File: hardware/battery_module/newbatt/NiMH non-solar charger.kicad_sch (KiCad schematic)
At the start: 23 parts, among them J14 Conn_01x01_Socket, J15 Conn_01x01_Socket, J16 Conn_01x01_Socket, J17 Conn_01x01_Socket, J18 Conn_01x01_Socket, J19 Conn_01x01_Socket, J20 Conn_01x01_Socket, J21 Conn_01x01_Socket, J4 Screw_Terminal_01x02, U1 BQ25172DSGR

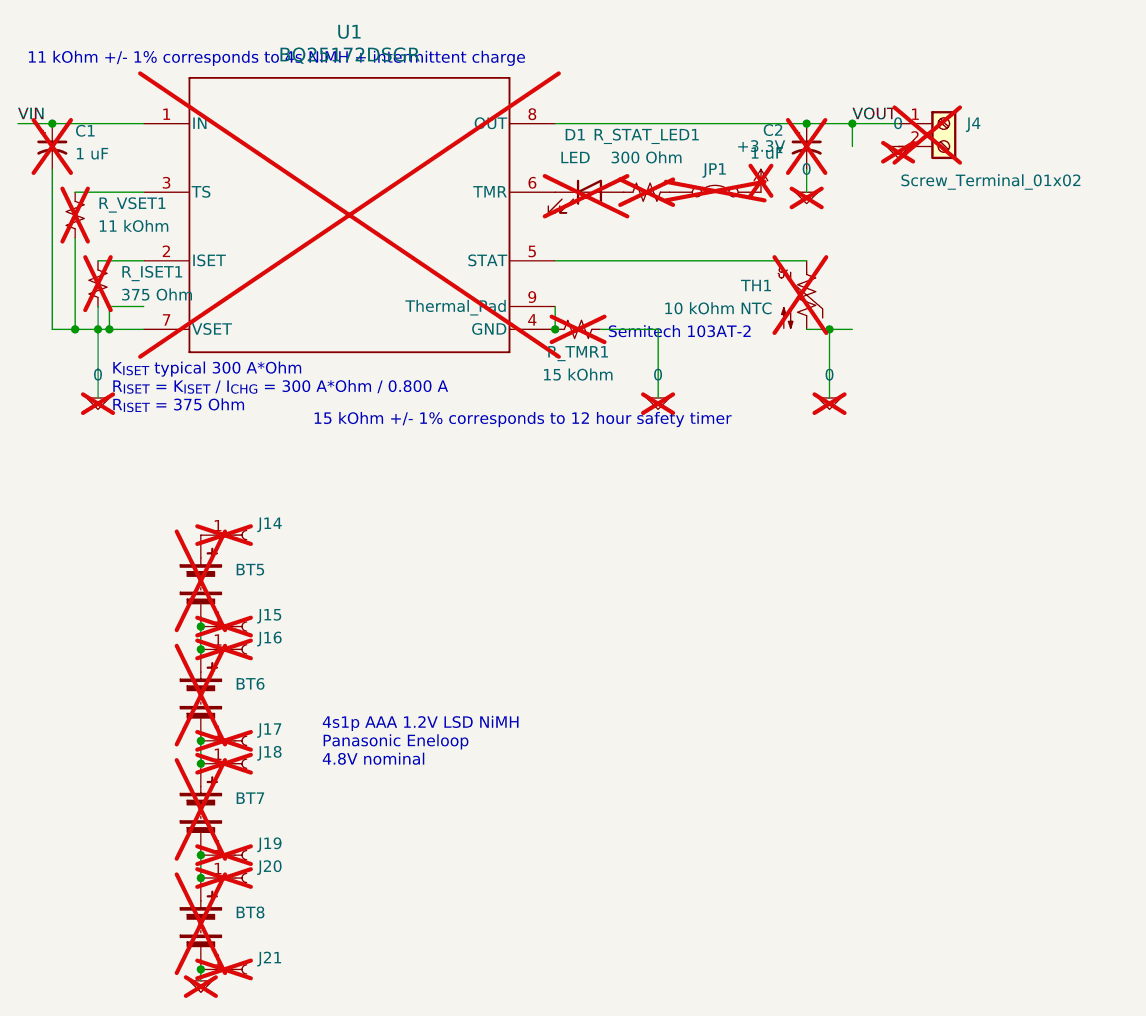
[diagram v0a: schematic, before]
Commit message: battery switch, fuse, and rerouted traces
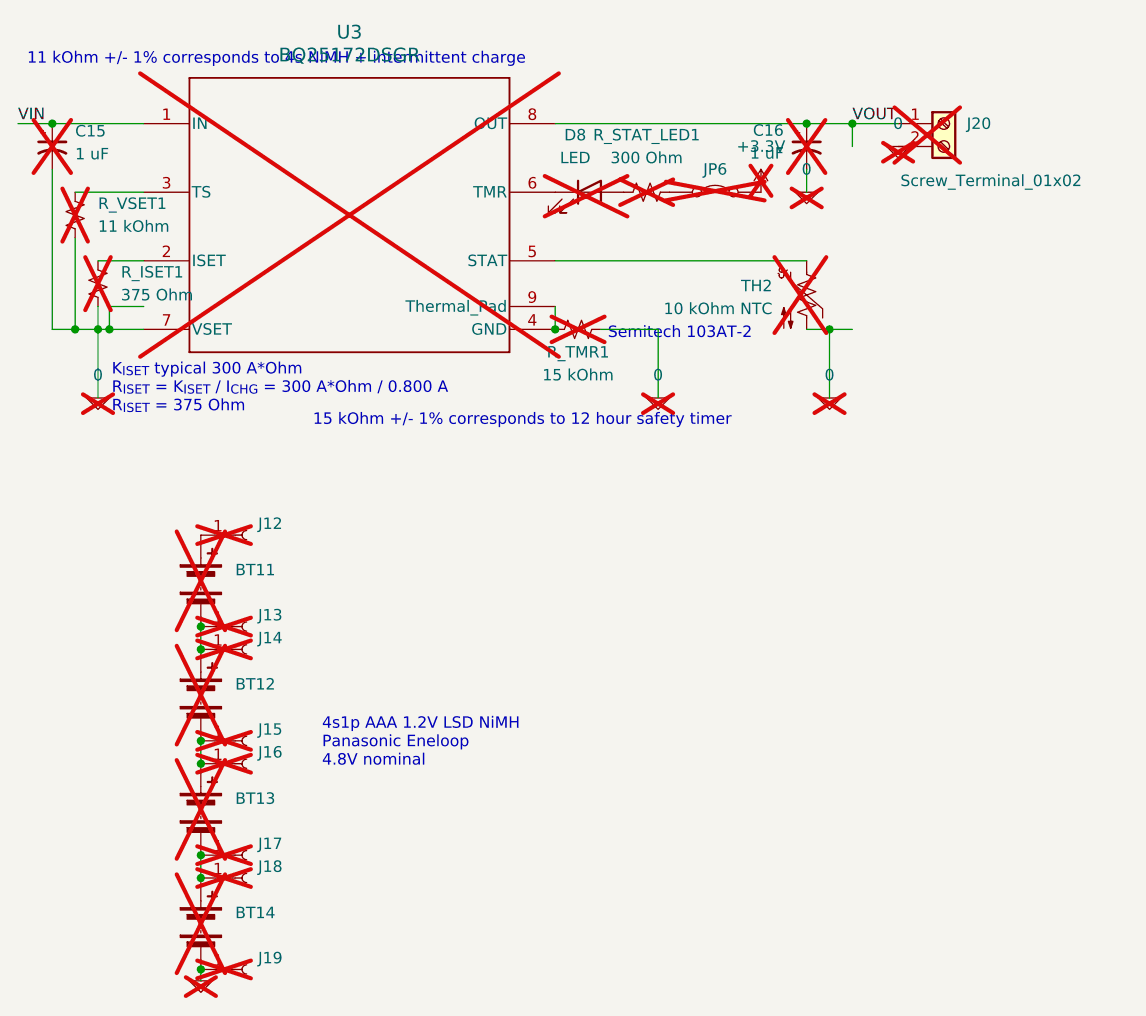
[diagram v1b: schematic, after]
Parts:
- renumbered BT5 to BT11, BT6 to BT12, BT7 to BT13, BT8 to BT14, C1 to C15, C2 to C16, D1 to D8, J14 to J12, J15 to J13, J16 to J14, J17 to J15, J18 to J16, J19 to J17, J20 to J18, J21 to J19, J4 to J20, JP1 to JP6, TH1 to TH2, U1 to U3
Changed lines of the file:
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@@
 		(dnp yes)
 		(fields_autoplaced yes)
-		(property "Reference" "#GND011"
+		(property "Reference" "#GND036"
 			(at 168.91 85.09 0)
 			(effects
@@
 			(project "newbatt"
 				(path "/492e8d1d-dcc5-45c6-a3d2-2dfd8a06477e/93fd5e6a-f298-4a43-8a46-dea204637830"
-					(reference "#GND011")
+					(reference "#GND036")
 					(unit 1)
 				)
@@
 		(on_board no)
 		(dnp yes)
-		(property "Reference" "JP1"
+		(property "Reference" "JP6"
 			(at 148.59 82.55 0)
 			(effects
@@
 			(project "newbatt"
 				(path "/492e8d1d-dcc5-45c6-a3d2-2dfd8a06477e/93fd5e6a-f298-4a43-8a46-dea204637830"
-					(reference "JP1")
+					(reference "JP6")
 					(unit 1)
 				)
@@
 		(dnp yes)
 		(fields_autoplaced yes)
-		(property "Reference" "#GND04"
+		(property "Reference" "#GND035"
 			(at 161.29 113.03 0)
 			(effects
@@
 			(project "newbatt"
 				(path "/492e8d1d-dcc5-45c6-a3d2-2dfd8a06477e/93fd5e6a-f298-4a43-8a46-dea204637830"
-					(reference "#GND04")
+					(reference "#GND035")
 					(unit 1)
 				)
@@
 		(dnp yes)
 		(fields_autoplaced yes)
-		(property "Reference" "J20"
+		(property "Reference" "J18"
 			(at 97.79 160.0199 0)
 			(effects
@@
 			(project "newbatt"
 				(path "/492e8d1d-dcc5-45c6-a3d2-2dfd8a06477e/93fd5e6a-f298-4a43-8a46-dea204637830"
-					(reference "J20")
+					(reference "J18")
 					(unit 1)
 				)
@@
 		(dnp yes)
 		(fields_autoplaced yes)
-		(property "Reference" "J15"
+		(property "Reference" "J13"
 			(at 97.79 132.0799 0)
 			(effects
@@
 			(project "newbatt"
 				(path "/492e8d1d-dcc5-45c6-a3d2-2dfd8a06477e/93fd5e6a-f298-4a43-8a46-dea204637830"
-					(reference "J15")
+					(reference "J13")
 					(unit 1)
 				)
@@
 		(dnp yes)
 		(fields_autoplaced yes)
-		(property "Reference" "#GND01"
+		(property "Reference" "#GND031"
 			(at 80.01 113.03 0)
 			(effects
@@
 			(project "newbatt"
 				(path "/492e8d1d-dcc5-45c6-a3d2-2dfd8a06477e/93fd5e6a-f298-4a43-8a46-dea204637830"
-					(reference "#GND01")
+					(reference "#GND031")
 					(unit 1)
 				)
@@
 		(on_board no)
 		(dnp yes)
-		(property "Reference" "C2"
+		(property "Reference" "C16"
 			(at 156.21 78.232 0)
 			(effects
@@
 			(project "newbatt"
 				(path "/492e8d1d-dcc5-45c6-a3d2-2dfd8a06477e/93fd5e6a-f298-4a43-8a46-dea204637830"
-					(reference "C2")
+					(reference "C16")
 					(unit 1)
 				)
@@
 		(dnp yes)
 		(fields_autoplaced yes)
-		(property "Reference" "#GND03"
+		(property "Reference" "#GND034"
 			(at 158.75 90.17 0)
 			(effects
@@
 			(project "newbatt"
 				(path "/492e8d1d-dcc5-45c6-a3d2-2dfd8a06477e/93fd5e6a-f298-4a43-8a46-dea204637830"
-					(reference "#GND03")
+					(reference "#GND034")
 					(unit 1)
 				)
@@
 		(dnp yes)
 		(fields_autoplaced yes)
-		(property "Reference" "D1"
+		(property "Reference" "D8"
 			(at 133.0325 78.74 0)
 			(effects
@@
 			(project "newbatt"
 				(path "/492e8d1d-dcc5-45c6-a3d2-2dfd8a06477e/93fd5e6a-f298-4a43-8a46-dea204637830"
-					(reference "D1")
+					(reference "D8")
 					(unit 1)
 				)
@@
 		(dnp yes)
 		(fields_autoplaced yes)
-		(property "Reference" "U1"
+		(property "Reference" "U3"
 			(at 107.95 67.31 0)
 			(effects
@@
 			(project "newbatt"
 				(path "/492e8d1d-dcc5-45c6-a3d2-2dfd8a06477e/93fd5e6a-f298-4a43-8a46-dea204637830"
-					(reference "U1")
+					(reference "U3")
 					(unit 1)
 				)
@@
 		(dnp yes)
 		(fields_autoplaced yes)
-		(property "Reference" "J16"
+		(property "Reference" "J14"
 			(at 97.79 134.6199 0)
 			(effects
@@
 			(project "newbatt"
 				(path "/492e8d1d-dcc5-45c6-a3d2-2dfd8a06477e/93fd5e6a-f298-4a43-8a46-dea204637830"
-					(reference "J16")
+					(reference "J14")
 					(unit 1)
 				)
@@
 		(dnp yes)
 		(fields_autoplaced yes)
-		(property "Reference" "#GND034"
+		(property "Reference" "#GND032"
 			(at 91.44 177.8 0)
 			(effects
@@
 			(project "newbatt"
 				(path "/492e8d1d-dcc5-45c6-a3d2-2dfd8a06477e/93fd5e6a-f298-4a43-8a46-dea204637830"
-					(reference "#GND034")
+					(reference "#GND032")
 					(unit 1)
 				)
@@
 		(dnp yes)
 		(fields_autoplaced yes)
-		(property "Reference" "J17"
+		(property "Reference" "J15"
 			(at 97.79 144.7799 0)
 			(effects
@@
 			(project "newbatt"
 				(path "/492e8d1d-dcc5-45c6-a3d2-2dfd8a06477e/93fd5e6a-f298-4a43-8a46-dea204637830"
-					(reference "J17")
+					(reference "J15")
 					(unit 1)
 				)
@@
 		(dnp yes)
 		(fields_autoplaced yes)
-		(property "Reference" "BT7"
+		(property "Reference" "BT13"
 			(at 95.25 152.4634 0)
 			(effects
@@
 			(project "newbatt"
 				(path "/492e8d1d-dcc5-45c6-a3d2-2dfd8a06477e/93fd5e6a-f298-4a43-8a46-dea204637830"
-					(reference "BT7")
+					(reference "BT13")
 					(unit 1)
 				)
@@
 		(dnp yes)
 		(fields_autoplaced yes)
-		(property "Reference" "J18"
+		(property "Reference" "J16"
 			(at 97.79 147.3199 0)
 			(effects
@@
 			(project "newbatt"
 				(path "/492e8d1d-dcc5-45c6-a3d2-2dfd8a06477e/93fd5e6a-f298-4a43-8a46-dea204637830"
-					(reference "J18")
+					(reference "J16")
 					(unit 1)
 				)
@@
 		(dnp yes)
 		(fields_autoplaced yes)
-		(property "Reference" "J19"
+		(property "Reference" "J17"
 			(at 97.79 157.4799 0)
 			(effects
@@
 			(project "newbatt"
 				(path "/492e8d1d-dcc5-45c6-a3d2-2dfd8a06477e/93fd5e6a-f298-4a43-8a46-dea204637830"
-					(reference "J19")
+					(reference "J17")
 					(unit 1)
 				)
@@
 		(dnp yes)
 		(fields_autoplaced yes)
-		(property "Reference" "J21"
+		(property "Reference" "J19"
 			(at 97.79 170.1799 0)
 			(effects
@@
 			(project "newbatt"
 				(path "/492e8d1d-dcc5-45c6-a3d2-2dfd8a06477e/93fd5e6a-f298-4a43-8a46-dea204637830"
-					(reference "J21")
+					(reference "J19")
 					(unit 1)
 				)
@@
 		(dnp yes)
 		(fields_autoplaced yes)
-		(property "Reference" "J14"
+		(property "Reference" "J12"
 			(at 97.79 121.9199 0)
 			(effects
@@
 			(project "newbatt"
 				(path "/492e8d1d-dcc5-45c6-a3d2-2dfd8a06477e/93fd5e6a-f298-4a43-8a46-dea204637830"
-					(reference "J14")
+					(reference "J12")
 					(unit 1)
 				)
@@
 		(dnp yes)
 		(fields_autoplaced yes)
-		(property "Reference" "BT8"
+		(property "Reference" "BT14"
 			(at 95.25 165.1634 0)
 			(effects
@@
 			(project "newbatt"
 				(path "/492e8d1d-dcc5-45c6-a3d2-2dfd8a06477e/93fd5e6a-f298-4a43-8a46-dea204637830"
-					(reference "BT8")
+					(reference "BT14")
 					(unit 1)
 				)
@@
 		(on_board no)
 		(dnp yes)
-		(property "Reference" "J4"
+		(property "Reference" "J20"
 			(at 176.53 77.4699 0)
 			(effects
@@
 			(project "newbatt"
 				(path "/492e8d1d-dcc5-45c6-a3d2-2dfd8a06477e/93fd5e6a-f298-4a43-8a46-dea204637830"
-					(reference "J4")
+					(reference "J20")
 					(unit 1)
 				)
@@
 		(dnp yes)
 		(fields_autoplaced yes)
-		(property "Reference" "BT6"
+		(property "Reference" "BT12"
 			(at 95.25 139.7634 0)
 			(effects
@@
 			(project "newbatt"
 				(path "/492e8d1d-dcc5-45c6-a3d2-2dfd8a06477e/93fd5e6a-f298-4a43-8a46-dea204637830"
-					(reference "BT6")
+					(reference "BT12")
 					(unit 1)
 				)
@@
 		(dnp yes)
 		(fields_autoplaced yes)
-		(property "Reference" "C1"
+		(property "Reference" "C15"
 			(at 77.47 78.3081 0)
 			(effects
@@
 			(project "newbatt"
 				(path "/492e8d1d-dcc5-45c6-a3d2-2dfd8a06477e/93fd5e6a-f298-4a43-8a46-dea204637830"
-					(reference "C1")
+					(reference "C15")
 					(unit 1)
 				)
@@
 		(dnp yes)
 		(fields_autoplaced yes)
-		(property "Reference" "BT5"
+		(property "Reference" "BT11"
 			(at 95.25 127.0634 0)
 			(effects
@@
 			(project "newbatt"
 				(path "/492e8d1d-dcc5-45c6-a3d2-2dfd8a06477e/93fd5e6a-f298-4a43-8a46-dea204637830"
-					(reference "BT5")
+					(reference "BT11")
 					(unit 1)
 				)
@@
 		(dnp yes)
 		(fields_autoplaced yes)
-		(property "Reference" "#GND02"
+		(property "Reference" "#GND033"
 			(at 142.24 113.03 0)
 			(effects
@@
 			(project "newbatt"
 				(path "/492e8d1d-dcc5-45c6-a3d2-2dfd8a06477e/93fd5e6a-f298-4a43-8a46-dea204637830"
-					(reference "#GND02")
+					(reference "#GND033")
 					(unit 1)
 				)
@@
 		(on_board no)
 		(dnp yes)
-		(property "Reference" "TH1"
+		(property "Reference" "TH2"
 			(at 154.94 95.504 0)
 			(effects
@@
 			(project "newbatt"
 				(path "/492e8d1d-dcc5-45c6-a3d2-2dfd8a06477e/93fd5e6a-f298-4a43-8a46-dea204637830"
-					(reference "TH1")
-					(unit 1)
-				)
+					(reference "TH2")
+					(unit 1)
+				)

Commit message: Updated BoM with LCSC, Digikey. Updated 18650 battery clip footprint with 67.2mm spacing for 65mm and 67mm cells
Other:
- title: (none) -> ENTS Node Battery Module
